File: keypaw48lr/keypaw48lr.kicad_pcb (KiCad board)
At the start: 2 copper layers, 147 x 102 mm, 118 parts, among them J1 Conn_01x02, J2 Conn_01x02, J3 Conn_01x02, J4 Conn_01x02, J5 Conn_01x02, J6 JD9613_OLED_FPC_Conn_01x10, J7 JD9613_OLED_FPC_Conn_01x10, J8 DXCL_S2002A_C, SW1 SW_SPDT, U1 nice_nano, U2 PAW3395, U3 TLV70019_SOT23-5, U4 TPS22917DBV

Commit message: fix: move oled fpc out of antenna range?
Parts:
- R4: moved to F.Cu
- SW1: moved to B.Cu
- moved TP1 45.4 mm to (95.9, 49.1)
- moved J1 40.6 mm to (89.8, 49.0)
- moved R4 35.0 mm to (107.9, 106.4), turned to 90 degrees
- moved J6 30.8 mm to (56.1, 101.8)
- moved J7 30.8 mm to (56.0, 101.8)
- moved SW1 27.5 mm to (82.9, 49.0), turned to 0 degrees
- moved R1 15.3 mm to (58.8, 58.7)
- moved TP2 12.7 mm to (71.2, 53.5)
- moved R2 11.1 mm to (52.5, 58.7)
- moved U1 10.9 mm to (55.7, 65.0)
- moved J2 9.81 mm to (72.5, 49.0)
- moved J8 6.40 mm to (123.3, 133.2)
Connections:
- U1 pad 10: CS_PAW -> CS_OLED
- U1 pad 18: ROW1 -> COL0
- U1 pad 19: COL0 -> COL1
- U1 pad 2: DS_OLED -> MOTION
- U1 pad 20: COL1 -> COL2
- U1 pad 21: COL2 -> ROW1
- U1 pad 5: CS_OLED -> SCK
- U1 pad 6: MOTION -> SDO
- U1 pad 7: SCK -> SDI
- U1 pad 8: SDO -> CS_PAW
- U1 pad 9: SDI -> DS_OLED
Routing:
- net GND: track 942.9 -> 997.7 mm, vias 89 -> 138
- net EINT: track 99.3 -> 143.5 mm, vias 2 -> 3
- net DS_OLED: track 10.8 -> 52.1 mm, vias 1 -> 2
- net CS_OLED: track 11.1 -> 46.4 mm
- net +3.3V: track 188.7 -> 154.1 mm, vias 4 -> 8
- net MOTION: track 126.8 -> 154.8 mm
- net COL2: track 192.3 -> 164.4 mm, vias 3 -> 1
- net SCK: track 125.6 -> 150.6 mm, vias 1 -> 4
- net SDO: track 131.2 -> 153.8 mm, vias 2 -> 3
- net ROW2: track 178.7 -> 156.3 mm, vias 1 -> 2
- net +BATT: track 15.0 -> 32.0 mm
- net CS_PAW: track 123.5 -> 139.8 mm
- net ROW0: track 136.9 -> 122.1 mm
- net SDI: track 141.7 -> 129.7 mm
- net V_peri: track 768.7 -> 759.6 mm, vias 8 -> 9
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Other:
- outline, holes or cut-outs redrawn

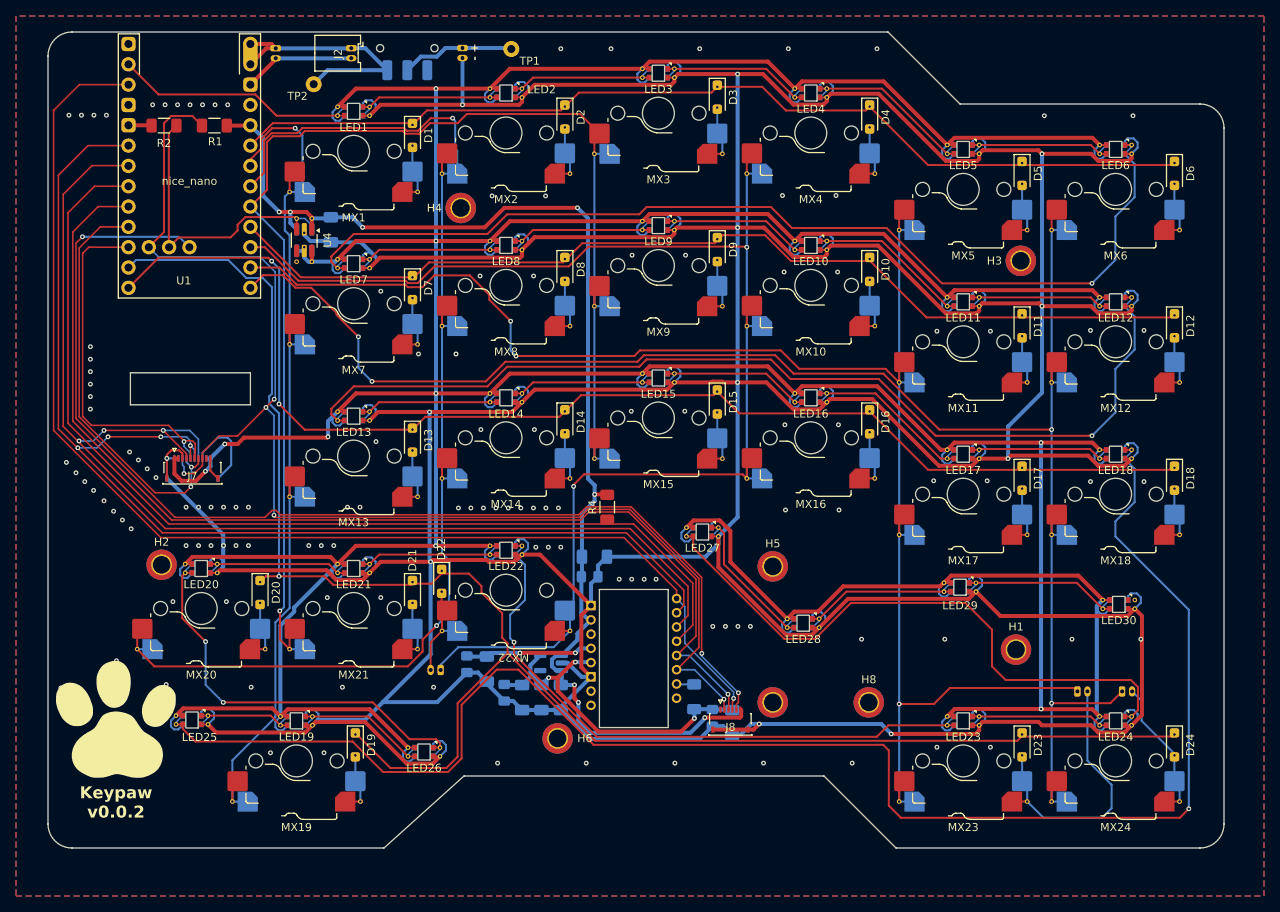
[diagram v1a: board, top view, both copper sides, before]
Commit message: fix: non-reverse-mountable V_peri components
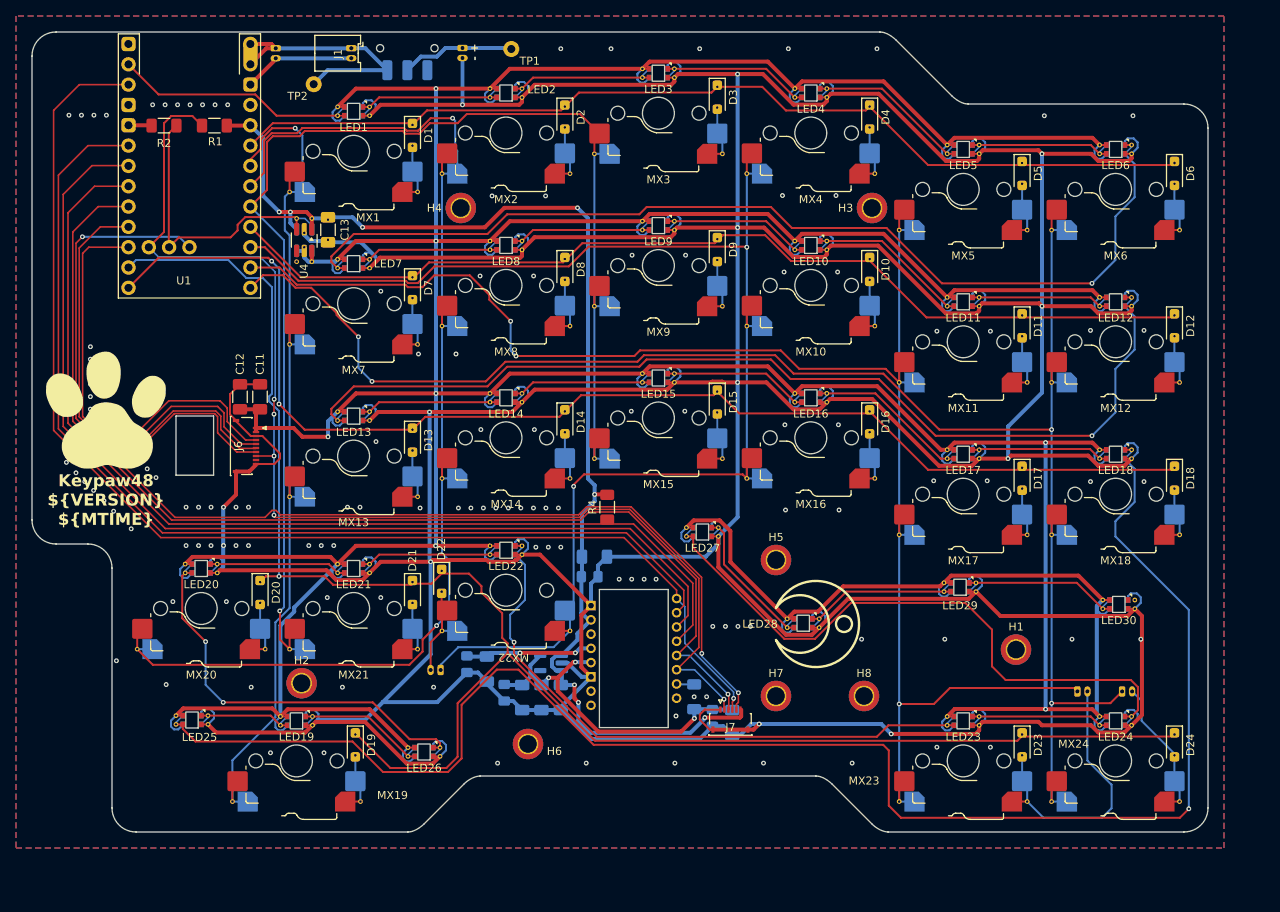
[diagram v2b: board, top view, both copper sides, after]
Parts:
- removed the J7 at (56.0, 101.8)
- added C11: 1uF, Capacitor_SMD:C_1206_3216Metric_Pad1.33x1.80mm_HandSolder, F.Cu at (64.5, 92.6)
- added C12: 10uF, Capacitor_SMD:C_1206_3216Metric_Pad1.33x1.80mm_HandSolder, F.Cu at (62.0, 92.6)
- C13: renamed from C11; footprint Capacitor_SMD:C_1206_3216Metric_Pad1.33x1.80mm_HandSolder -> MX_SW_HS_REV:C_1206_3216Metric_Pad1.33x1.80mm_HandSolder_REV
- J6: moved to F.Cu
- moved G*** 38.7 mm to (45.2, 94.2) (x2)
- moved H2 22.9 mm to (69.7, 128.4)
- moved H3 19.7 mm to (141.0, 69.0)
- moved J6 7.13 mm to (62.5, 98.8), turned to -90 degrees
- moved H6 3.77 mm to (98.0, 136.0)
- moved H8 1.00 mm to (140.0, 130.0)
- moved H7 0.89 mm to (129.0, 130.0)
- moved H5 0.89 mm to (129.0, 113.0)
- moved C13 0.36 mm to (73.0, 71.7)
- renumbered J2 to J1, J1 to J2, J8 to J7
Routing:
- net NRESET: track 165.6 -> 150.4 mm
- net V_peri: track 759.6 -> 749.4 mm, vias 9 -> 7
- net SCK: track 150.6 -> 159.2 mm, vias 4 -> 2
- net CS_OLED: track 46.4 -> 53.7 mm, vias 1 -> 0
- net DS_OLED: track 52.1 -> 56.4 mm, vias 2 -> 0
- net SDO: track 153.8 -> 158.0 mm, vias 3 -> 2
- net GND: track 997.7 -> 1001.1 mm, vias 138 -> 140
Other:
- board size 147 x 102 mm -> 147 x 100 mm
- board text added: "Keypaw48 ${VERSION} ${MTIME}"
- board text removed: "Keypaw v0.0.2"
